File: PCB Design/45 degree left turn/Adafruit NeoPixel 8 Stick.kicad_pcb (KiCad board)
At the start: 2 copper layers, 26.2 x 21.4 mm, 4 parts, among them CN1 1X4SMT, CN2 1X4SMT

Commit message: arrows
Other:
- board text removed: "DIN"
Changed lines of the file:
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@@
       (net 2 "GND") (pinfunction "4") (pintype "bidirectional") (solder_mask_margin 0.1016))
   )
+  (gr_line (start 130.556 106.426) (end 137.414 103.632) (layer "B.SilkS") (width 0.12))
+  (gr_line (start 137.414 103.632) (end 136.144 105.918) (layer "B.SilkS") (width 0.12))
+  (gr_line (start 137.414 103.632) (end 134.366 102.87) (layer "B.SilkS") (width 0.12))
   (gr_line (start 131.064 113.792) (end 122.428 113.792) (layer "Edge.Cuts") (width 0.05))
   (gr_line (start 131.243152 98.487726) (end 137.349726 92.381152) (layer "Edge.Cuts") (width 0.05))
@@
     (effects (font (size 1.143 1.143) (thickness 0.127)) (justify left bottom mirror))
   )
-  (gr_text "4-7VDC" (at 128.9812 107.0864) (layer "B.SilkS")
-    (effects (font (size 1.143 1.143) (thickness 0.127)) (justify right top mirror))
-  )
   (gr_text "DOUT" (at 155.194 131.4704 270) (layer "B.SilkS")
     (effects (font (size 1.143 1.143) (thickness 0.127)) (justify left bottom mirror))
@@
     (effects (font (size 1.143 1.143) (thickness 0.127)) (justify left bottom mirror))
   )
-  (gr_text "DIN" (at 128.9812 105.0544) (layer "B.SilkS")
-    (effects (font (size 1.143 1.143) (thickness 0.127)) (justify right top mirror))
-  )
   (gr_text "GND" (at 157.734 131.4704 270) (layer "B.SilkS")
     (effects (font (size 1.143 1.143) (thickness 0.127)) (justify left bottom mirror))
   )
-  (gr_text "GND" (at 128.9812 102.5144) (layer "B.SilkS")
-    (effects (font (size 1.143 1.143) (thickness 0.127)) (justify right top mirror))
-  )
-  (gr_text "GND" (at 128.9812 109.1184) (layer "B.SilkS")
-    (effects (font (size 1.143 1.143) (thickness 0.127)) (justify right top mirror))
-  )
   (segment (start 140.208 103.100741) (end 140.95837 102.35037) (width 0.25) (layer "F.Cu") (net 1))

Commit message: 6 pin
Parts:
- moved CN1 2.42 mm to (140.0, 103.0)
- moved D1 1.70 mm to (128.8, 108.0)
- moved D2 1.30 mm to (138.4, 104.1)
- moved CN2 0.52 mm to (126.9, 107.4)
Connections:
- CN1 pad 1: GND -> Net-(CN1-Pad1)
- CN1 pad 2: Net-(D2-Pad2) -> Net-(CN1-Pad2)
- CN1 pad 3: +5V -> GND
- CN1 pad 4: GND -> Net-(CN1-Pad4)
- D2 pad 2: Net-(D2-Pad2) -> Net-(CN1-Pad4)
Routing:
- net Net-(CN1-Pad2): track 0.00 -> 12.5 mm
- net Net-(CN1-Pad1): track 0.00 -> 10.0 mm
- net +5V: track 18.9 -> 22.8 mm
- net Net-(CN2-Pad3): track 3.67 -> 0.00 mm
- net Net-(CN1-Pad4): track 0.00 -> 3.66 mm, vias 0 -> 1
- net Net-(D1-Pad2): track 5.96 -> 6.87 mm
- net Net-(D2-Pad2): vias 1 -> 0
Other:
- board size 26.2 x 21.4 mm -> 27.9 x 26.4 mm
- board text removed: "4-7VDC"
- board text removed: "DOUT"
- board text removed: "GND"

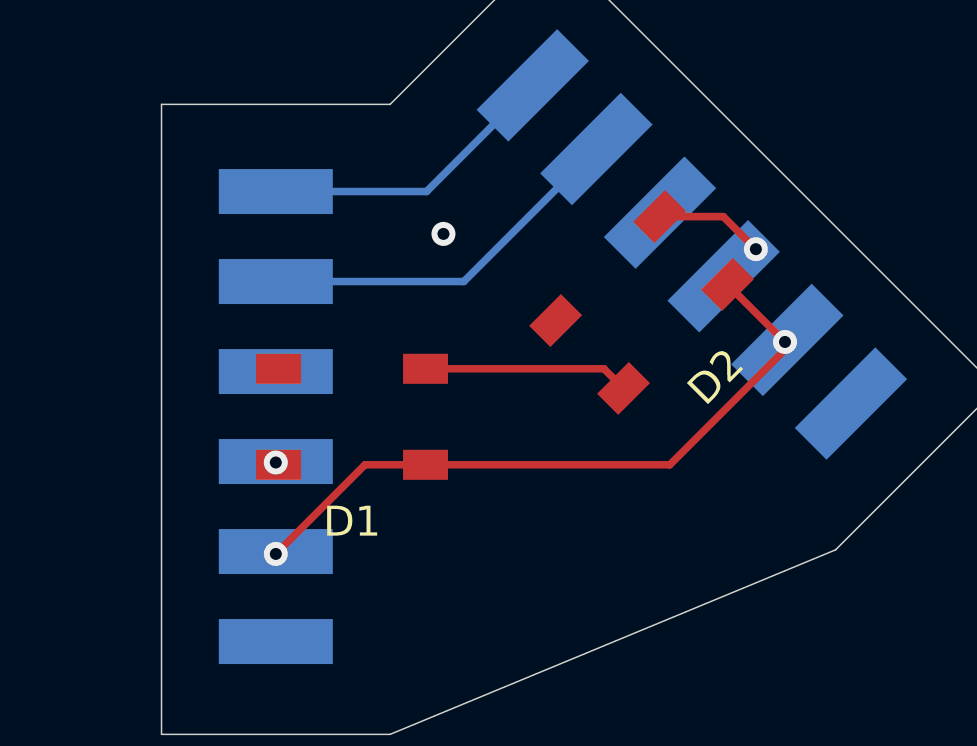
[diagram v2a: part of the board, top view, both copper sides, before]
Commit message: move vias off pads
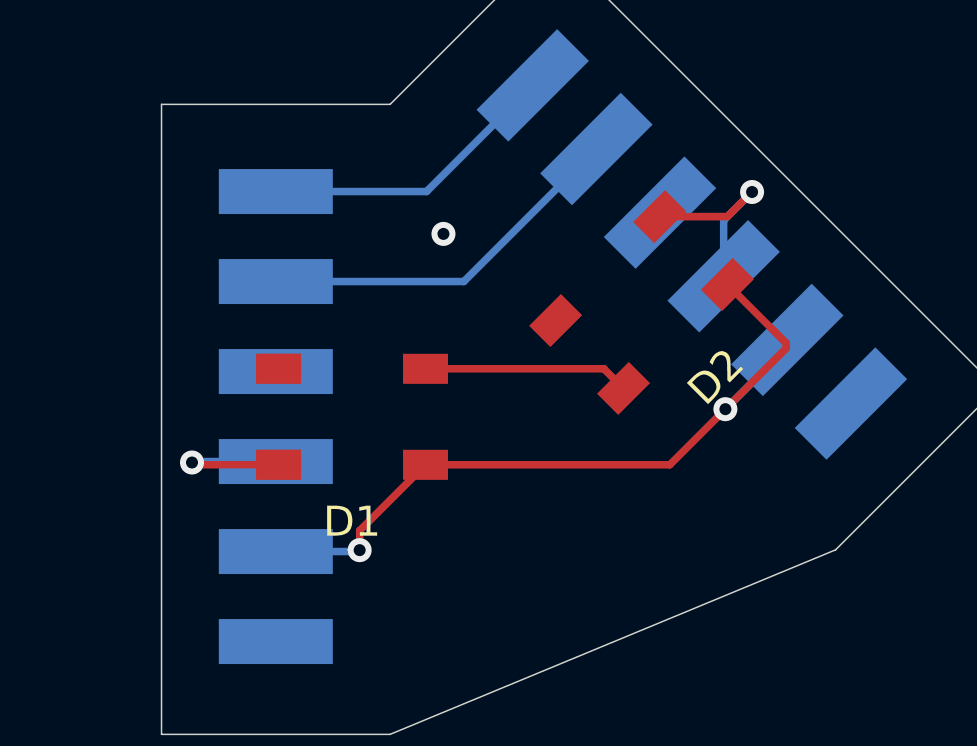
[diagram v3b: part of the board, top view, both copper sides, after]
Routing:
- net Net-(CN2-Pad3): track 0.00 -> 5.72 mm
- net +5V: track 22.8 -> 26.3 mm
- net Net-(CN1-Pad4): track 3.66 -> 6.62 mm
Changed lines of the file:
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@@
   (gr_line (start 130.048004 118.536) (end 144.897241 112.385243) (layer "Edge.Cuts") (width 0.05))
   (gr_line (start 122.428 97.536) (end 130.048 97.536) (layer "Edge.Cuts") (width 0.05))
+  (segment (start 143.256 105.501178) (end 141.293782 103.538959) (width 0.25) (layer "F.Cu") (net 1))
+  (segment (start 131.228 109.55) (end 129.032 111.746) (width 0.25) (layer "F.Cu") (net 1))
   (segment (start 131.228 109.55) (end 139.37 109.55) (width 0.25) (layer "F.Cu") (net 1))
-  (segment (start 143.256 105.664) (end 143.256 105.501177) (width 0.25) (layer "F.Cu") (net 1))
-  (segment (start 143.210411 105.455589) (end 141.293782 103.538959) (width 0.25) (layer "F.Cu") (net 1))
-  (segment (start 143.256 105.501177) (end 143.210411 105.455589) (width 0.25) (layer "F.Cu") (net 1))
   (segment (start 139.37 109.55) (end 143.256 105.664) (width 0.25) (layer "F.Cu") (net 1))
-  (segment (start 129.21 109.55) (end 131.228 109.55) (width 0.25) (layer "F.Cu") (net 1))
-  (segment (start 126.238 112.522) (end 129.21 109.55) (width 0.25) (layer "F.Cu") (net 1))
-  (via (at 143.210411 105.455589) (size 0.8) (drill 0.4) (layers "F.Cu" "B.Cu") (net 1))
-  (via (at 126.238 112.522) (size 0.8) (drill 0.4) (layers "F.Cu" "B.Cu") (net 1))
+  (segment (start 143.256 105.664) (end 143.256 105.501178) (width 0.25) (layer "F.Cu") (net 1))
+  (segment (start 129.032 111.746) (end 129.032 112.395) (width 0.25) (layer "F.Cu") (net 1))
+  (via (at 141.224 107.696) (size 0.8) (drill 0.4) (layers "F.Cu" "B.Cu") (net 1))
+  (via (at 129.032 112.395) (size 0.8) (drill 0.4) (layers "F.Cu" "B.Cu") (net 1))
+  (segment (start 128.985 112.442) (end 129.032 112.395) (width 0.25) (layer "B.Cu") (net 1))
+  (segment (start 126.238 112.442) (end 128.985 112.442) (width 0.25) (layer "B.Cu") (net 1))
+  (segment (start 141.224 107.696) (end 143.287869 105.632131) (width 0.25) (layer "B.Cu") (net 1))
+  (segment (start 143.287869 105.632131) (end 143.287869 105.387712) (width 0.25) (layer "B.Cu") (net 1))
   (via (at 131.826 101.854) (size 0.8) (drill 0.4) (layers "F.Cu" "B.Cu") (free) (net 2))
   (segment (start 126.238 103.442) (end 132.505659 103.442) (width 0.25) (layer "B.Cu") (net 3))
   (segment (start 132.505659 103.442) (end 136.923908 99.023751) (width 0.25) (layer "B.Cu") (net 3))
-  (via (at 126.238 109.474) (size 0.8) (drill 0.4) (layers "F.Cu" "B.Cu") (net 4))
+  (segment (start 123.52 109.55) (end 123.444 109.474) (width 0.25) (layer "F.Cu") (net 4))
+  (segment (start 126.328 109.55) (end 123.52 109.55) (width 0.25) (layer "F.Cu") (net 4))
+  (via (at 123.444 109.474) (size 0.8) (drill 0.4) (layers "F.Cu" "B.Cu") (net 4))
+  (segment (start 123.444 109.474) (end 123.476 109.442) (width 0.25) (layer "B.Cu") (net 4))
+  (segment (start 123.476 109.442) (end 126.238 109.442) (width 0.25) (layer "B.Cu") (net 4))
   (segment (start 137.175177 106.35) (end 137.828959 107.003782) (width 0.25) (layer "F.Cu") (net 5))
   (segment (start 131.228 106.35) (end 137.175177 106.35) (width 0.25) (layer "F.Cu") (net 5))
   (segment (start 131.263019 100.442) (end 134.802588 96.902431) (width 0.25) (layer "B.Cu") (net 6))
   (segment (start 126.238 100.442) (end 131.263019 100.442) (width 0.25) (layer "B.Cu") (net 6))
-  (segment (start 139.031041 101.276218) (end 141.154218 101.276218) (width 0.25) (layer "F.Cu") (net 7))
-  (segment (start 141.154218 101.276218) (end 142.24 102.362) (width 0.25) (layer "F.Cu") (net 7))
-  (via (at 142.24 102.362) (size 0.8) (drill 0.4) (layers "F.Cu" "B.Cu") (net 7))
+  (segment (start 139.031041 101.276218) (end 141.293782 101.276218) (width 0.25) (layer "F.Cu") (net 7))
+  (segment (start 141.293782 101.276218) (end 142.113 100.457) (width 0.25) (layer "F.Cu") (net 7))
+  (via (at 142.113 100.457) (size 0.8) (drill 0.4) (layers "F.Cu" "B.Cu") (net 7))
+  (segment (start 141.166549 101.403451) (end 141.166549 103.266392) (width 0.25) (layer "B.Cu") (net 7))
+  (segment (start 142.113 100.457) (end 141.166549 101.403451) (width 0.25) (layer "B.Cu") (net 7))
   (zone (net 2) (net_name "GND") (layers F&B.Cu) (hatch edge 0.508)
     (priority 6)
